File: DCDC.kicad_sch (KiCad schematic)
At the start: 44 parts, among them U5 AP64502QSP-13, U7 AP64502, U8 AP22653W6, U9 CH221K

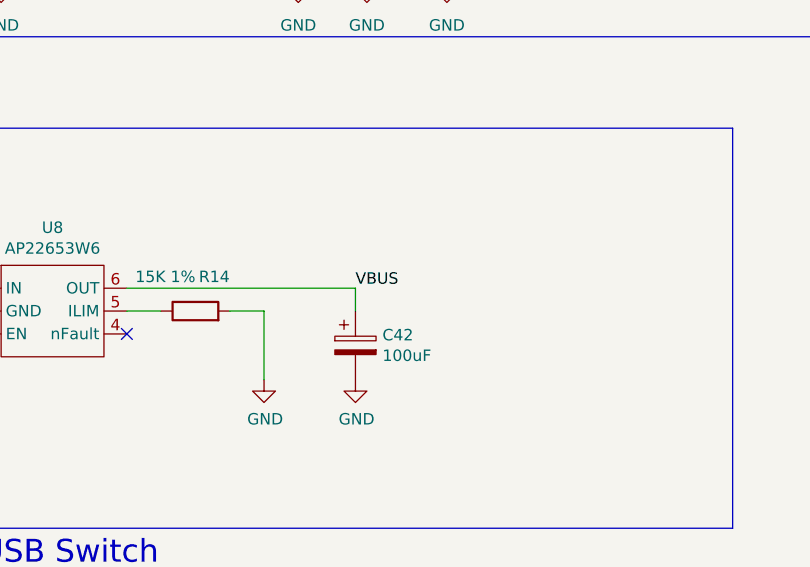
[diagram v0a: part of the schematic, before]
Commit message: remove usb
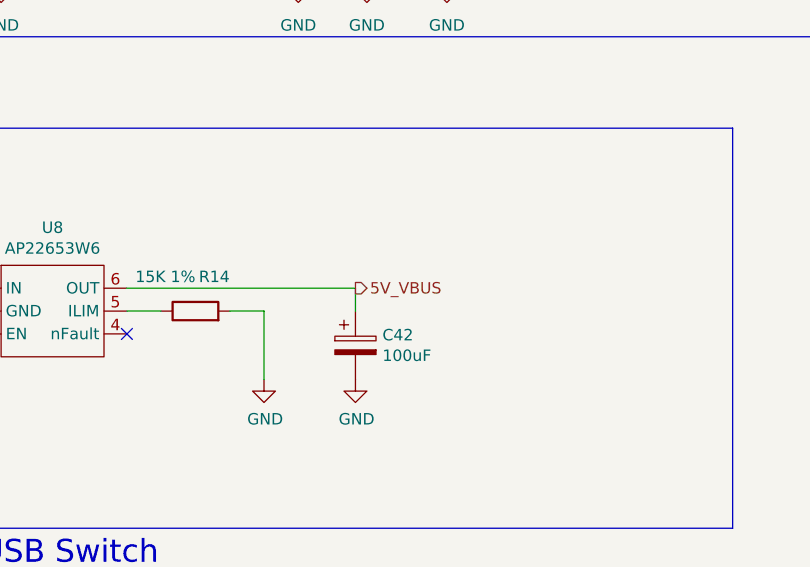
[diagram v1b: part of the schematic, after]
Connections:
- net VBUS: no longer C42.1, U8.6 (OUT)
- new net 5V_VBUS: C42.1, U8.6 (OUT)
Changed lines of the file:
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@@
-		)
-	)
-	(label "VBUS"
-		(at 119.38 144.78 0)
-		(fields_autoplaced yes)
-		(effects
-			(font
-				(size 1.27 1.27)
-			)
-			(justify left bottom)
 		)
 	)
@@
 		)
 	)
+	(hierarchical_label "5V_VBUS"
+		(shape output)
+		(at 119.38 144.78 0)
+		(fields_autoplaced yes)
+		(effects
+			(font
+				(size 1.27 1.27)
+			)
+			(justify left)
+		)
+	)

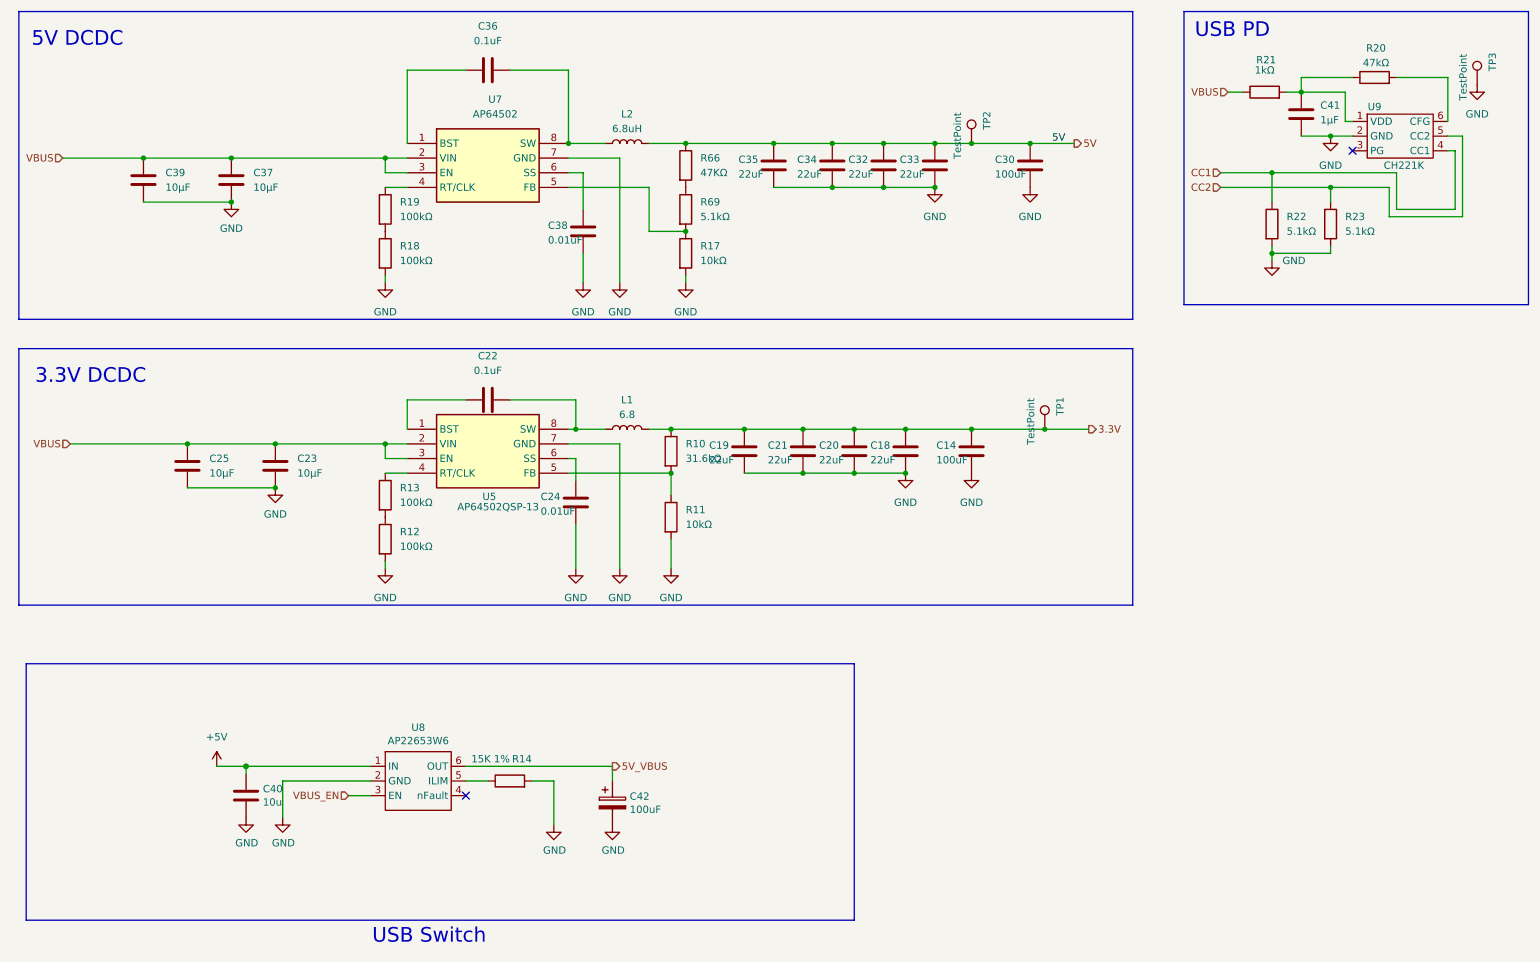
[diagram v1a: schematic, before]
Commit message: change USB2.0
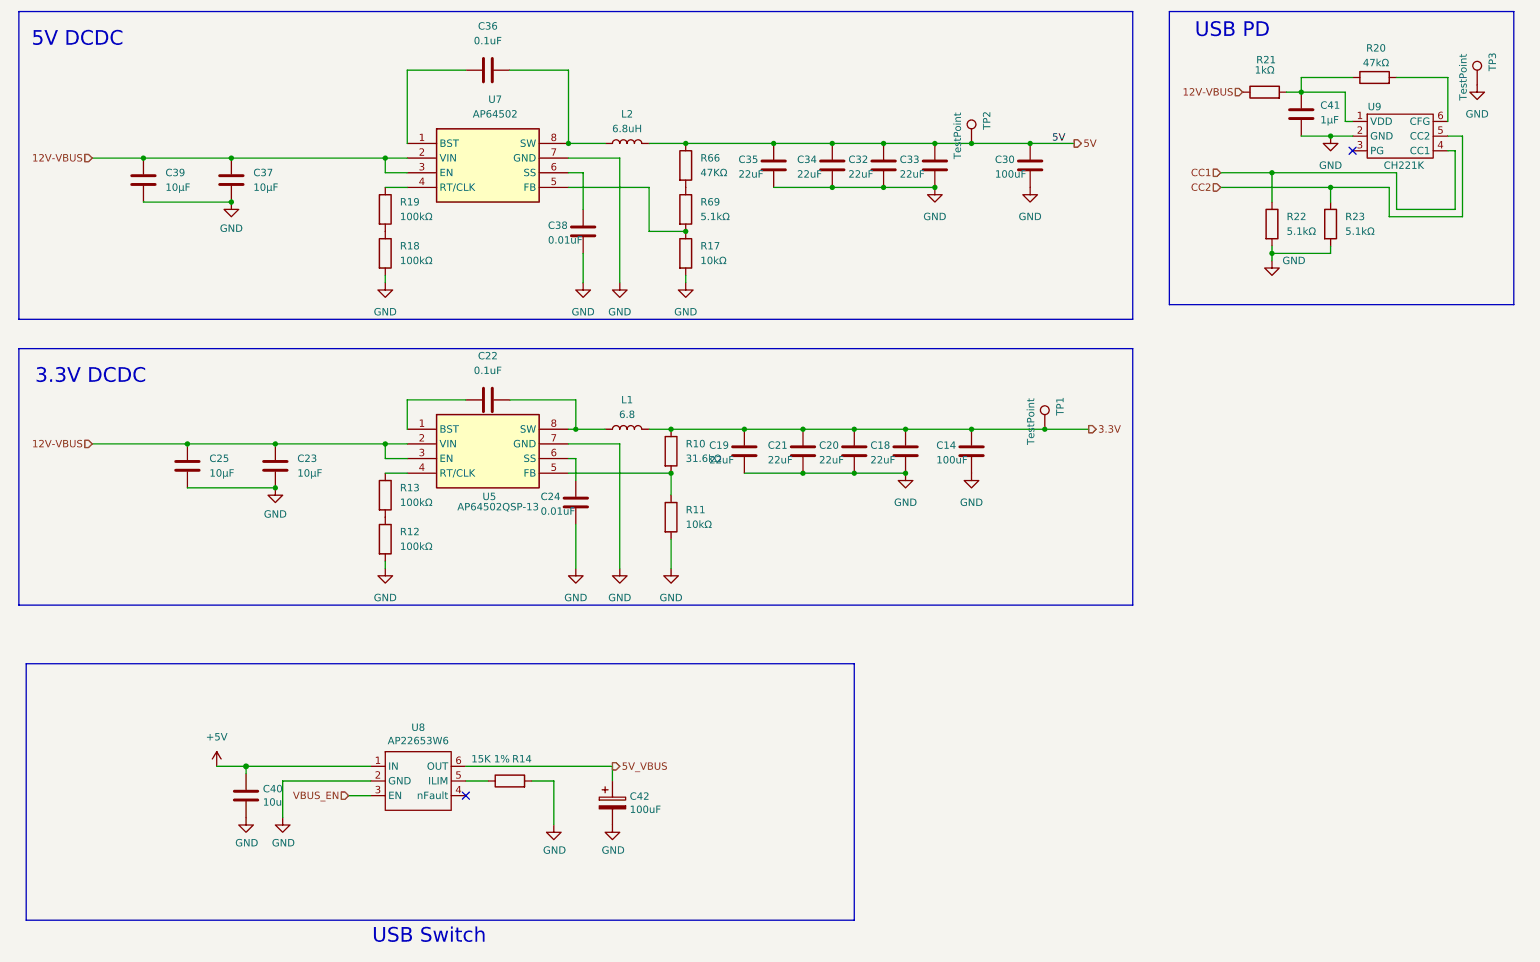
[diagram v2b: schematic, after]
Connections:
- net VBUS renamed 12V-VBUS
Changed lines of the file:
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@@
 	(wire
 		(pts
-			(xy 24.13 39.37) (xy 38.1 39.37)
+			(xy 29.21 39.37) (xy 38.1 39.37)
 		)
 		(stroke
@@
 	(wire
 		(pts
-			(xy 25.4 88.9) (xy 45.72 88.9)
+			(xy 29.21 88.9) (xy 45.72 88.9)
 		)
 		(stroke
@@
 		(pts
 			(xy 129.54 86.36) (xy 142.24 86.36)
-		)
-		(stroke
-			(width 0)
-			(type default)
-		)
-	)
-	(wire
-		(pts
-			(xy 226.06 27.94) (xy 228.6 27.94)
 		)
 		(stroke
@@
 	)
 	(rectangle
-		(start 218.44 13.97)
-		(end 278.13 64.77)
+		(start 215.9 13.97)
+		(end 275.59 64.77)
 		(stroke
 			(width 0)
@@
 	(label "5V"
 		(at 195.58 36.83 0)
-		(fields_autoplaced yes)
 		(effects
 			(font
@@
 		(shape input)
 		(at 73.66 149.86 180)
-		(fields_autoplaced yes)
 		(effects
 			(font
@@
 		(shape output)
 		(at 201.93 86.36 0)
-		(fields_autoplaced yes)
 		(effects
 			(font
@@
 		)
 	)
-	(hierarchical_label "VBUS"
+	(hierarchical_label "12V-VBUS"
 		(shape input)
-		(at 24.13 39.37 180)
-		(fields_autoplaced yes)
+		(at 29.21 39.37 180)
 		(effects
 			(font
@@
 		)
 	)
-	(hierarchical_label "VBUS"
+	(hierarchical_label "12V-VBUS"
 		(shape input)
-		(at 226.06 27.94 180)
-		(fields_autoplaced yes)
+		(at 228.6 27.94 180)
 		(effects
 			(font
@@
 		(shape output)
 		(at 199.39 36.83 0)
-		(fields_autoplaced yes)
 		(effects
 			(font
@@
 		(shape input)
 		(at 224.79 44.45 180)
-		(fields_autoplaced yes)
 		(effects
 			(font
@@
 		(shape input)
 		(at 224.79 41.91 180)
-		(fields_autoplaced yes)
 		(effects
 			(font
@@
 		)
 	)
-	(hierarchical_label "VBUS"
+	(hierarchical_label "12V-VBUS"
 		(shape input)
-		(at 25.4 88.9 180)
-		(fields_autoplaced yes)
+		(at 29.21 88.9 180)
 		(effects
 			(font
@@
 		(shape output)
 		(at 119.38 144.78 0)
-		(fields_autoplaced yes)
-		(effects
-			(font
+		(effects
+			(font

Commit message: end route
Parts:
- renumbered C30 to C26, C32 to C28, C33 to C29, R17 to R15, R18 to R16, R19 to R17, R66 to R60, R69 to R61
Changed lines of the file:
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@@
 		(dnp no)
 		(fields_autoplaced yes)
-		(property "Reference" "R19"
+		(property "Reference" "R17"
 			(at 82.55 46.9899 0)
 			(effects
@@
 			(project ""
 				(path "/dd07ab80-a59c-44f4-ac7d-849e21e1384e/eab21d37-4422-449e-812a-90afc228ebcf"
-					(reference "R19")
+					(reference "R17")
 					(unit 1)
 				)
@@
 		(dnp no)
 		(fields_autoplaced yes)
-		(property "Reference" "R18"
+		(property "Reference" "R16"
 			(at 82.55 54.6099 0)
 			(effects
@@
 			(project "mainboard4"
 				(path "/dd07ab80-a59c-44f4-ac7d-849e21e1384e/eab21d37-4422-449e-812a-90afc228ebcf"
-					(reference "R18")
+					(reference "R16")
 					(unit 1)
 				)
@@
 		(dnp no)
 		(fields_autoplaced yes)
-		(property "Reference" "R69"
+		(property "Reference" "R61"
 			(at 134.62 46.9899 0)
 			(effects
@@
 			(project "mainboard4"
 				(path "/dd07ab80-a59c-44f4-ac7d-849e21e1384e/eab21d37-4422-449e-812a-90afc228ebcf"
-					(reference "R69")
+					(reference "R61")
 					(unit 1)
 				)
@@
 		(dnp no)
 		(fields_autoplaced yes)
-		(property "Reference" "R66"
+		(property "Reference" "R60"
 			(at 134.62 39.3699 0)
 			(effects
@@
 			(project "mainboard4"
 				(path "/dd07ab80-a59c-44f4-ac7d-849e21e1384e/eab21d37-4422-449e-812a-90afc228ebcf"
-					(reference "R66")
+					(reference "R60")
 					(unit 1)
 				)
@@
 		(on_board yes)
 		(dnp no)
-		(property "Reference" "C32"
+		(property "Reference" "C28"
 			(at 160.274 39.624 0)
 			(effects
@@
 			(project "mainboard4"
 				(path "/dd07ab80-a59c-44f4-ac7d-849e21e1384e/eab21d37-4422-449e-812a-90afc228ebcf"
-					(reference "C32")
+					(reference "C28")
 					(unit 1)
 				)
@@
 		(on_board yes)
 		(dnp no)
-		(property "Reference" "C33"
+		(property "Reference" "C29"
 			(at 169.164 39.624 0)
 			(effects
@@
 			(project "mainboard4"
 				(path "/dd07ab80-a59c-44f4-ac7d-849e21e1384e/eab21d37-4422-449e-812a-90afc228ebcf"
-					(reference "C33")
+					(reference "C29")
 					(unit 1)
 				)
@@
 		(on_board yes)
 		(dnp no)
-		(property "Reference" "C30"
+		(property "Reference" "C26"
 			(at 185.674 39.624 0)
 			(effects
@@
 			(project "mainboard4"
 				(path "/dd07ab80-a59c-44f4-ac7d-849e21e1384e/eab21d37-4422-449e-812a-90afc228ebcf"
-					(reference "C30")
+					(reference "C26")
 					(unit 1)
 				)
@@
 		(dnp no)
 		(fields_autoplaced yes)
-		(property "Reference" "R17"
+		(property "Reference" "R15"
 			(at 134.62 54.6099 0)
 			(effects
@@
 			(project "mainboard4"
 				(path "/dd07ab80-a59c-44f4-ac7d-849e21e1384e/eab21d37-4422-449e-812a-90afc228ebcf"
-					(reference "R17")
-					(unit 1)
-				)
+					(reference "R15")
+					(unit 1)
+				)

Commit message: データをアップロード
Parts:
- removed C40: 10u, Capacitor_SMD:C_0805_2012Metric, symbol Device:C
- removed C42: 100uF, Capacitor_Tantalum_SMD:CP_EIA-7343-31_Kemet-D, symbol Device:C_Polarized
- removed R14: 15K 1%, Resistor_SMD:R_0603_1608Metric_Pad0.98x0.95mm_HandSolder, symbol Device:R
- removed R60: 47KΩ, Resistor_SMD:R_0603_1608Metric_Pad0.98x0.95mm_HandSolder, symbol Device:R
- removed U8: AP22653W6, Package_TO_SOT_SMD:SOT-23-6, symbol CM5IO:AP2553W6
- added C72, C73, C74, C75: 10u, Capacitor_SMD:C_0603_1608Metric_Pad1.08x0.95mm_HandSolder, symbol Device:C
- added C83, C88: 10u, Capacitor_SMD:C_0805_2012Metric, symbol Device:C
- added C91: 22pF, Capacitor_SMD:C_0603_1608Metric_Pad1.08x0.95mm_HandSolder, symbol Device:C
- added L3: 2.2uH, Inductor_SMD:L_1210_3225Metric_Pad1.42x2.65mm_HandSolder, symbol Device:L
- added R50, R51: 100kΩ, Resistor_SMD:R_0603_1608Metric_Pad0.98x0.95mm_HandSolder, symbol Device:R
- added U14: AP3445LW6-7, Package_TO_SOT_SMD:SOT-23-6_Handsoldering, symbol CM5IO:AP3441SHE-7B
- R12: renamed from R22; footprint Resistor_SMD:R_0603_1608Metric_Pad0.98x0.95mm_HandSolder -> Resistor_SMD:R_0402_1005Metric_Pad0.72x0.64mm_HandSolder
- R13: renamed from R23; footprint Resistor_SMD:R_0603_1608Metric_Pad0.98x0.95mm_HandSolder -> Resistor_SMD:R_0402_1005Metric_Pad0.72x0.64mm_HandSolder
- R40: renamed from R11; footprint Resistor_SMD:R_0603_1608Metric_Pad0.98x0.95mm_HandSolder -> Resistor_SMD:R_0402_1005Metric_Pad0.72x0.64mm_HandSolder
- R54: renamed from R61; value 5.1kΩ -> 51.2kΩ; footprint Resistor_SMD:R_0603_1608Metric_Pad0.98x0.95mm_HandSolder -> Resistor_SMD:R_0402_1005Metric_Pad0.72x0.64mm_HandSolder
- R56: renamed from R15; footprint Resistor_SMD:R_0603_1608Metric_Pad0.98x0.95mm_HandSolder -> Resistor_SMD:R_0402_1005Metric_Pad0.72x0.64mm_HandSolder
- renumbered C14 to C18, C18 to C19, C19 to C20, C20 to C22, C22 to C23, C23 to C24, C24 to C27, C25 to C30, C26 to C31, C28 to C32, C29 to C33, C35 to C34, C34 to C35, R20 to R10, R21 to R11, R10 to R39, R12 to R41, R13 to R42, R17 to R8, R16 to R9, U7 to U6, U9 to U8
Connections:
- net 5V is gone; now on net +5V: C31.2, C32.2, C33.2, C34.2, C35.2, L2.2, TP2.1
- net +5V: now also R54.1, C83.1, C88.1, U14.1 (EN), U14.4 (VIN)
- net GND: now also C72.2, C73.2, C74.2, C75.2, C83.2, C88.2, R50.2, U14.2 (GND)
- net 12V-VBUS renamed +12V
- net 3.3V renamed +3.3V
- new net: C91.2, R50.1, R51.2, U14.6 (FB)
- new net: L3.1, U14.3 (LX)
- new net +1.2V: C72.1, C73.1, C74.1, C75.1, C91.1, L3.2, R51.1
- no-connect marks 2 -> 1
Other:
- note added: "1.2V DCDC"
- note added: "3.3V PCIe DCDC"
- note removed: "3.3V DCDC"
- note removed: "USB Switch"
- moved on the sheet: C24, R54, R56
